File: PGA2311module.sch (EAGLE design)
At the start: 15 parts, among them IC1 PGA2311P

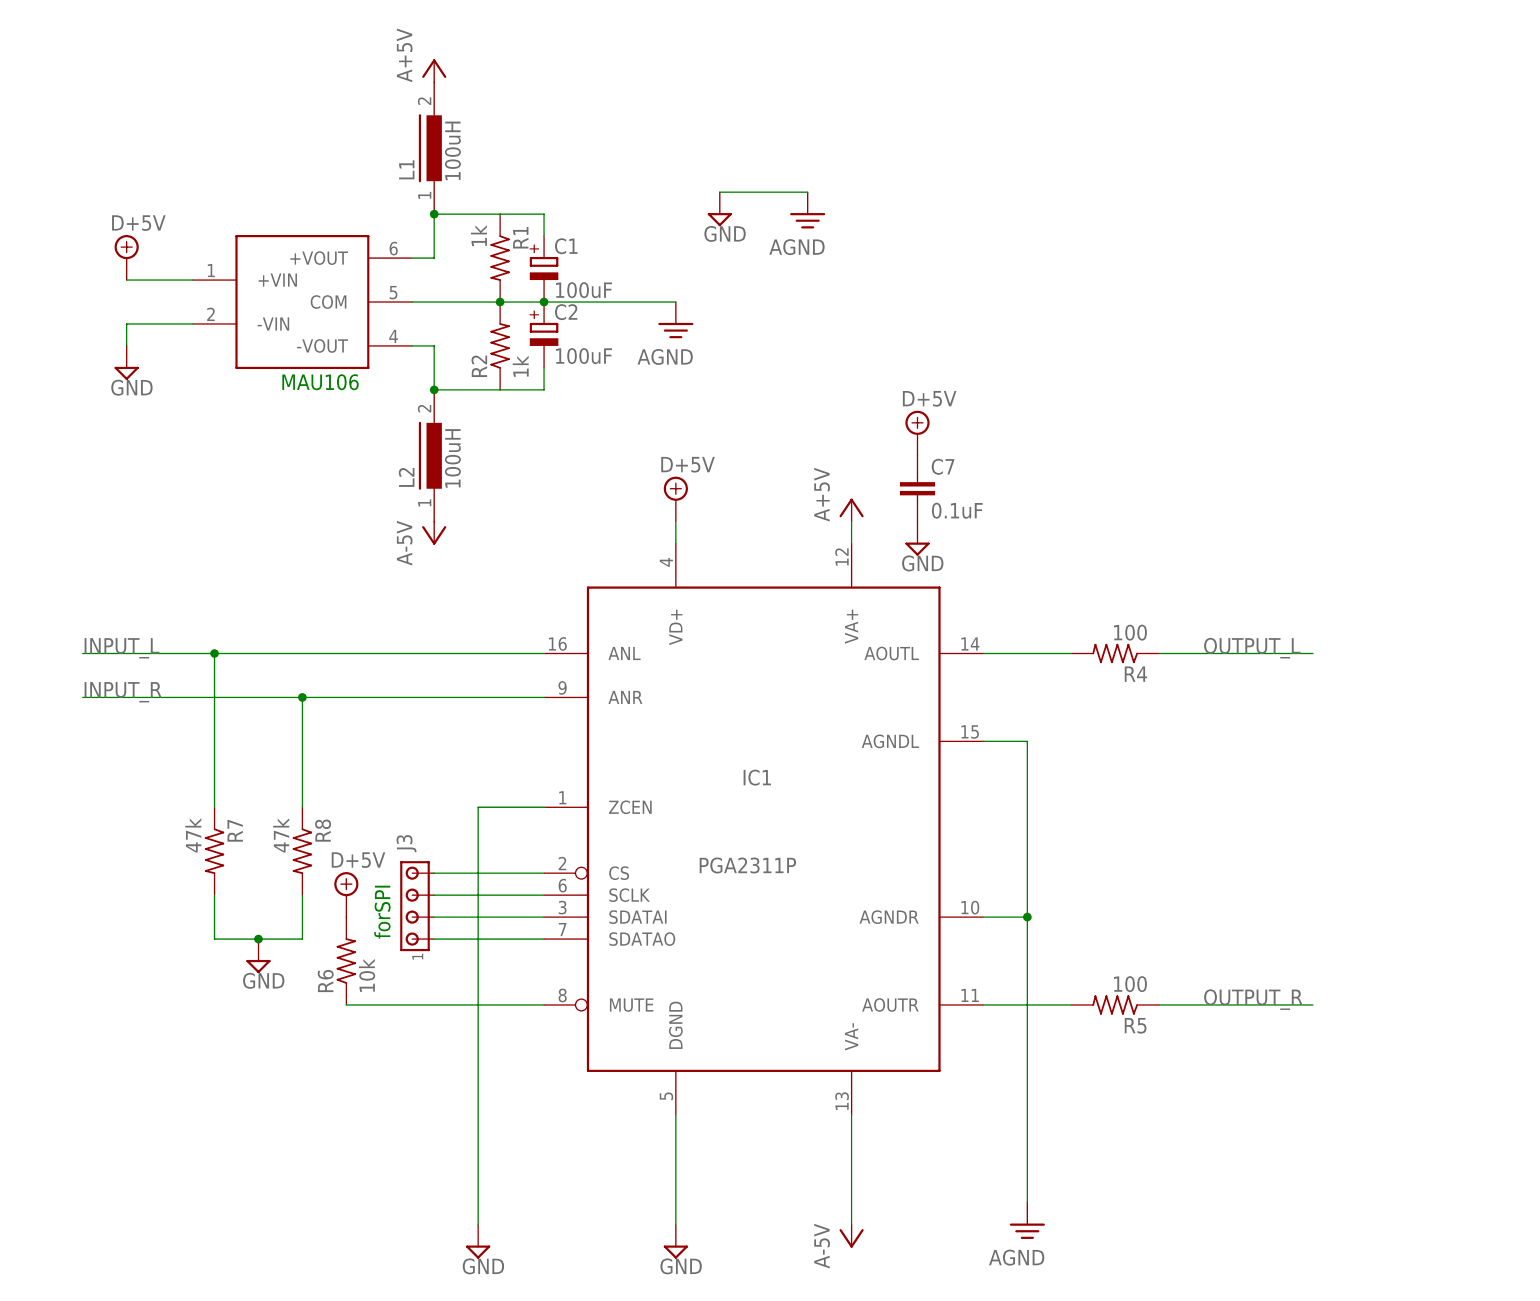
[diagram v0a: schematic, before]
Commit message: 電源周りのパスコンを追加。
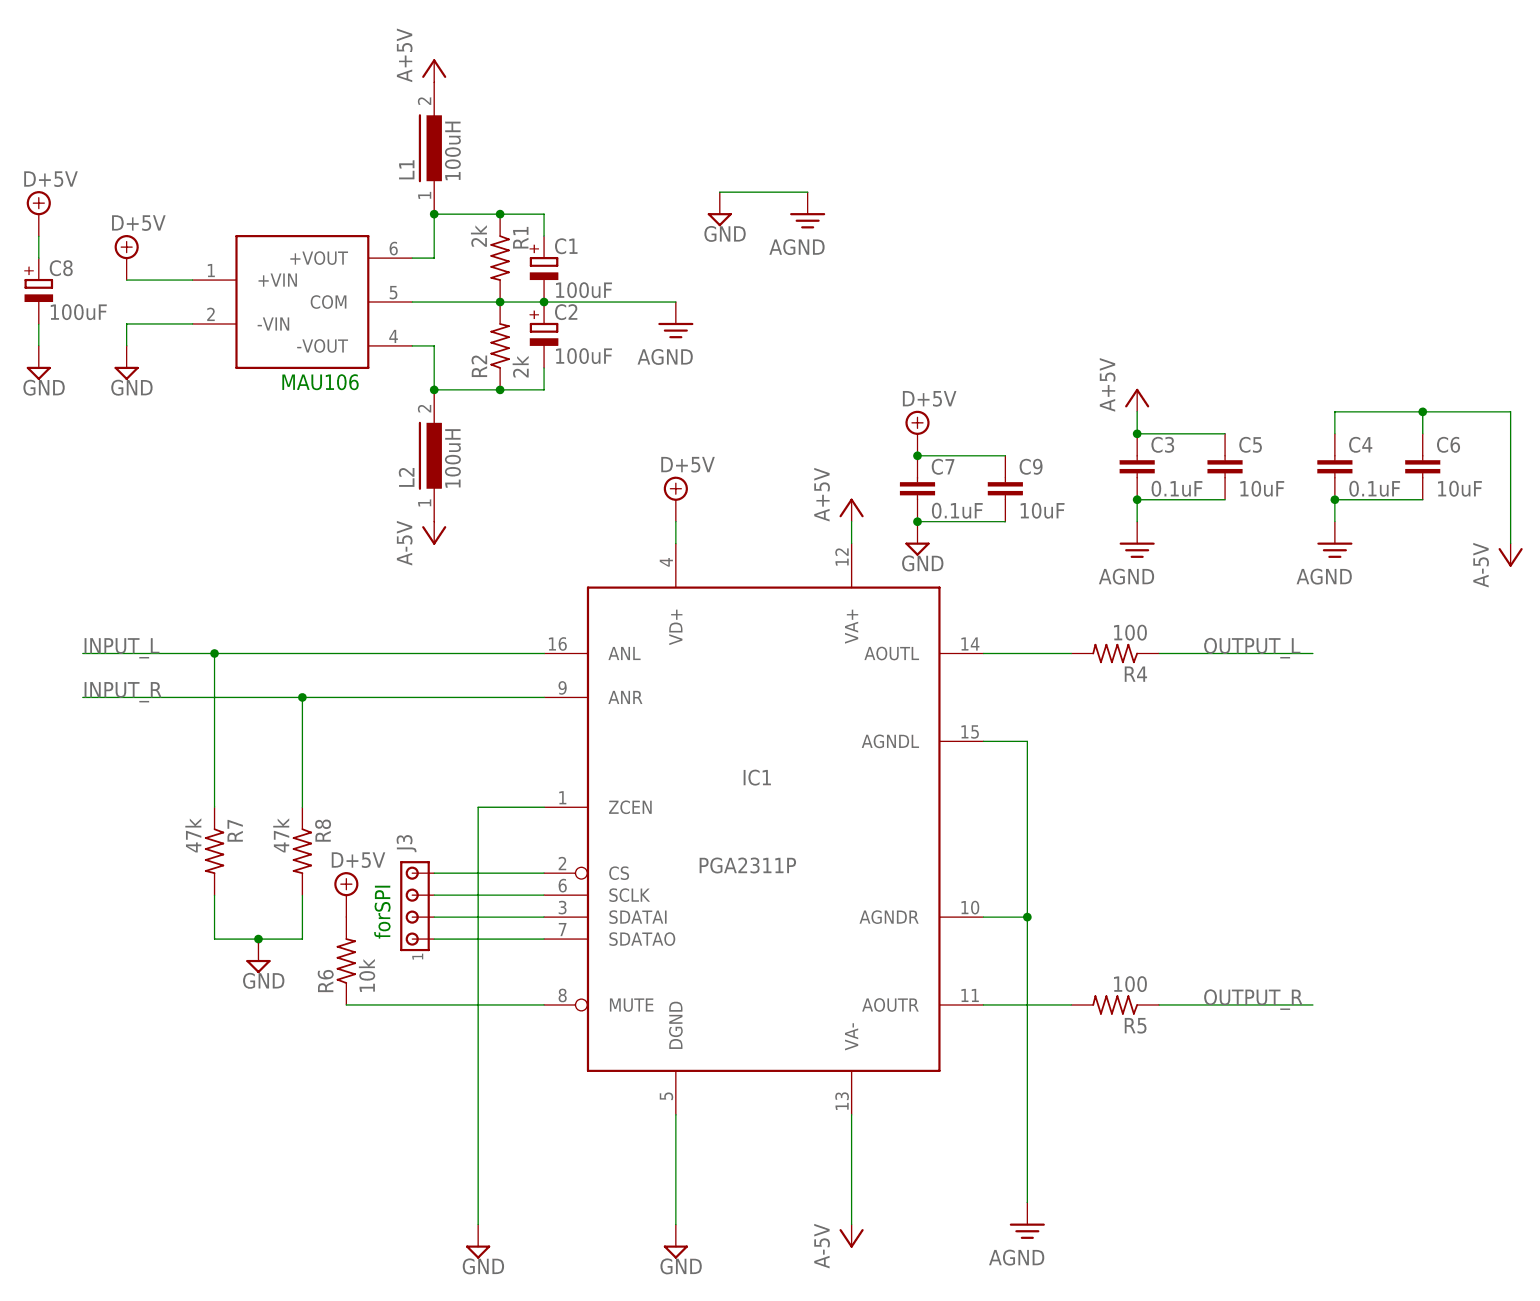
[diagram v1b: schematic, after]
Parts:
- added C3, C4: 0.1uF, rcl:C-EU050-030X075
- added C5, C6, C9: 10uF, rcl:C-EU050-030X075
- added C8: 100uF, rcl:CPOL-EUE5-8.5
- R1, R2: value 1k -> 2k
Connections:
- net +5V: now also C8.+, C9.1
- net -5V: now also C4.1, C6.1
- net GND: now also C8.-, C9.2
- net PE: now also C3.2, C4.2, C5.2, C6.2
- net VCC: now also C3.1, C5.1
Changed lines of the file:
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@@
 <part name="J3" library="con-amp" deviceset="MTA04-156" device=""/>
 <part name="U$1" library="MAU106" deviceset="MAU106" device=""/>
-<part name="R1" library="resistor" deviceset="R-US_" device="0411/15" value="1k"/>
-<part name="R2" library="resistor" deviceset="R-US_" device="0411/15" value="1k"/>
+<part name="R1" library="resistor" deviceset="R-US_" device="0411/15" value="2k"/>
+<part name="R2" library="resistor" deviceset="R-US_" device="0411/15" value="2k"/>
 <part name="C1" library="rcl" deviceset="CPOL-EU" device="E5-8.5" value="100uF"/>
 <part name="C2" library="rcl" deviceset="CPOL-EU" device="E5-8.5" value="100uF"/>
 <part name="L1" library="inductors" deviceset="82114R" device="" value="100uH"/>
 <part name="L2" library="inductors" deviceset="82114R" device="" value="100uH"/>
+<part name="P+3" library="supply1" deviceset="VCC" device="" value="A+5V"/>
+<part name="P-3" library="supply1" deviceset="-5V" device="" value="A-5V"/>
+<part name="C3" library="rcl" deviceset="C-EU" device="050-030X075" value="0.1uF"/>
+<part name="C4" library="rcl" deviceset="C-EU" device="050-030X075" value="0.1uF"/>
+<part name="SUPPLY2" library="supply2" deviceset="PE" device="" value="AGND"/>
+<part name="SUPPLY3" library="supply2" deviceset="PE" device="" value="AGND"/>
+<part name="C5" library="rcl" deviceset="C-EU" device="050-030X075" value="10uF"/>
+<part name="C6" library="rcl" deviceset="C-EU" device="050-030X075" value="10uF"/>
+<part name="C8" library="rcl" deviceset="CPOL-EU" device="E5-8.5" value="100uF"/>
+<part name="SUPPLY4" library="supply2" deviceset="+5V" device="" value="D+5V"/>
+<part name="SUPPLY5" library="supply2" deviceset="GND" device=""/>
+<part name="C9" library="rcl" deviceset="C-EU" device="050-030X075" value="10uF"/>
 </parts>
 <sheets>
@@
 <instance part="L1" gate="1" x="2.54" y="157.48" rot="R90"/>
 <instance part="L2" gate="1" x="2.54" y="121.92" rot="R90"/>
+<instance part="P+3" gate="VCC" x="83.82" y="129.54"/>
+<instance part="P-3" gate="1" x="127" y="109.22"/>
+<instance part="C3" gate="G$1" x="83.82" y="121.92"/>
+<instance part="C4" gate="G$1" x="106.68" y="121.92"/>
+<instance part="SUPPLY2" gate="PE" x="83.82" y="111.76"/>
+<instance part="SUPPLY3" gate="PE" x="106.68" y="111.76"/>
+<instance part="C5" gate="G$1" x="93.98" y="121.92"/>
+<instance part="C6" gate="G$1" x="116.84" y="121.92"/>
+<instance part="C8" gate="G$1" x="-43.18" y="142.24"/>
+<instance part="SUPPLY4" gate="+5V" x="-43.18" y="149.86"/>
+<instance part="SUPPLY5" gate="GND" x="-43.18" y="132.08"/>
+<instance part="C9" gate="G$1" x="68.58" y="119.38"/>
 </instances>
 <busses>
@@
 <pinref part="SUPPLY21" gate="GND" pin="GND"/>
 <pinref part="C7" gate="G$1" pin="2"/>
+<pinref part="C9" gate="G$1" pin="2"/>
+<wire x1="68.58" y1="114.3" x2="58.42" y2="114.3" width="0.1524" layer="91"/>
+<junction x="58.42" y="114.3"/>
 </segment>
 <segment>
@@
 <junction x="-17.78" y="66.04"/>
 </segment>
+<segment>
+<pinref part="C8" gate="G$1" pin="-"/>
+<pinref part="SUPPLY5" gate="GND" pin="GND"/>
+<wire x1="-43.18" y1="137.16" x2="-43.18" y2="134.62" width="0.1524" layer="91"/>
+</segment>
 </net>
 <net name="+5V" class="0">
@@
 <pinref part="C7" gate="G$1" pin="1"/>
 <pinref part="SUPPLY1" gate="+5V" pin="+5V"/>
+<pinref part="C9" gate="G$1" pin="1"/>
+<wire x1="58.42" y1="121.92" x2="68.58" y2="121.92" width="0.1524" layer="91"/>
+<junction x="58.42" y="121.92"/>
+</segment>
+<segment>
+<pinref part="SUPPLY4" gate="+5V" pin="+5V"/>
+<pinref part="C8" gate="G$1" pin="+"/>
+<wire x1="-43.18" y1="147.32" x2="-43.18" y2="144.78" width="0.1524" layer="91"/>
 </segment>
 </net>
@@
 <pinref part="C1" gate="G$1" pin="-"/>
 </segment>
+<segment>
+<pinref part="C3" gate="G$1" pin="2"/>
+<pinref part="SUPPLY2" gate="PE" pin="PE"/>
+<wire x1="83.82" y1="116.84" x2="83.82" y2="114.3" width="0.1524" layer="91"/>
+<pinref part="C5" gate="G$1" pin="2"/>
+<wire x1="93.98" y1="116.84" x2="83.82" y2="116.84" width="0.1524" layer="91"/>
+<junction x="83.82" y="116.84"/>
+</segment>
+<segment>
+<pinref part="C4" gate="G$1" pin="2"/>
+<pinref part="SUPPLY3" gate="PE" pin="PE"/>
+<wire x1="106.68" y1="116.84" x2="106.68" y2="114.3" width="0.1524" layer="91"/>
+<pinref part="C6" gate="G$1" pin="2"/>
+<wire x1="106.68" y1="116.84" x2="116.84" y2="116.84" width="0.1524" layer="91"/>
+<junction x="106.68" y="116.84"/>
+</segment>
 </net>
 <net name="INPUT_R" class="0">
@@
 <pinref part="P+1" gate="VCC" pin="VCC"/>
 </segment>
+<segment>
+<pinref part="P+3" gate="VCC" pin="VCC"/>
+<pinref part="C3" gate="G$1" pin="1"/>
+<wire x1="83.82" y1="127" x2="83.82" y2="124.46" width="0.1524" layer="91"/>
+<pinref part="C5" gate="G$1" pin="1"/>
+<wire x1="83.82" y1="124.46" x2="93.98" y2="124.46" width="0.1524" layer="91"/>
+<junction x="83.82" y="124.46"/>
+</segment>
 </net>
 <net name="-5V" class="0">
@@
 <pinref part="L2" gate="1" pin="1"/>
 <pinref part="P-2" gate="1" pin="-5V"/>
+</segment>
+<segment>
+<pinref part="C4" gate="G$1" pin="1"/>
+<wire x1="106.68" y1="124.46" x2="106.68" y2="127" width="0.1524" layer="91"/>
+<pinref part="P-3" gate="1" pin="-5V"/>
+<wire x1="106.68" y1="127" x2="116.84" y2="127" width="0.1524" layer="91"/>
+<wire x1="116.84" y1="127" x2="127" y2="127" width="0.1524" layer="91"/>
+<wire x1="127" y1="127" x2="127" y2="111.76" width="0.1524" layer="91"/>
+<pinref part="C6" gate="G$1" pin="1"/>
+<wire x1="116.84" y1="124.46" x2="116.84" y2="127" width="0.1524" layer="91"/>
+<junction x="116.84" y="127"/>
 </segment>
 </net>
@@
 <pinref part="L1" gate="1" pin="1"/>
 <junction x="2.54" y="149.86"/>
+<junction x="10.16" y="149.86"/>
 </segment>
 </net>
@@
 <pinref part="L2" gate="1" pin="2"/>
 <junction x="2.54" y="129.54"/>
-</segment>
-</net>
+<junction x="10.16" y="129.54"/>
+</segment>
+</net>
